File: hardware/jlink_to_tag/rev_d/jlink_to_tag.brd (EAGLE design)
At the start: 50.8 x 76.2 mm, 39 parts, among them J2 JLINK_6PIN_TAG-CON, J3 JLINK_6PIN_TAG-CON, J4 JLINK_6PIN_TAG-CON, J5 JLINK_6PIN_TAG-CON, J6 JLINK_6PIN_TAG-CON, J7 JLINK_6PIN_TAG-CON, J8 JLINK_6PIN_TAG-CON, J9 JLINK_6PIN_TAG-CON, U1 LT1763CS8-3.3

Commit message: getting more traces in
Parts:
- added D2, D3, D4, D5, D6, D7, D8, D9: BLUE, SparkFun-LED:LED-0603
- added R10, R11, R12, R13, R14, R15, R16, R9: 470, SparkFun-Passives:0603-RES
- added S10, S20, S4, S5, S6, S7, S8, S9: PTS645SM43SMTR92, switches:PTS645
- moved S1 62.0 mm to (78.7, 26.9)
- moved S2 62.0 mm to (73.2, 33.8)
- moved S3 62.0 mm to (83.8, 33.8)
- moved C1 21.5 mm to (-16.9, 49.3)
- moved C2 21.5 mm to (-12.2, 57.8)
- moved C3 21.5 mm to (-16.3, 57.8)
- moved D1 21.5 mm to (-13.8, 48.1)
- moved LOGO1 21.5 mm to (-15.4, 43.6)
- moved R1 21.5 mm to (-16.9, 47.2)
- moved U1 21.5 mm to (-15.1, 53.7)
- moved H2 20.2 mm to (60.2, 72.4)
- moved H4 20.2 mm to (60.2, 3.81)
- moved J6 20.2 mm to (60.2, 15.2)
- moved J7 20.2 mm to (60.2, 30.5)
- moved J9 20.2 mm to (60.2, 61.0)
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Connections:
- new net N$10: D8.C, R15.1
- new net N$11: D9.C, R16.1
- new net N$2: D2.C, R9.1
- new net N$5: D3.C, R10.1
- new net N$6: D4.C, R11.1
- new net N$7: D5.C, R12.1
- new net N$8: D6.C, R13.1
- new net N$9: D7.C, R14.1
- net !RST0: now also S4.3, S4.4
- net !RST1: now also S5.3, S5.4
- net !RST2: now also S6.3, S6.4
- net !RST3: now also S7.3, S7.4
- net !RST4: now also S8.3, S8.4
- net !RST5: now also S9.3, S9.4
- net !RST6: now also S10.3, S10.4
- net !RST7: now also S20.3, S20.4
- net EN0: now also D2.A
- net EN1: now also D3.A
- net EN2: now also D4.A
- net EN3: now also D5.A
- net EN4: now also D6.A
- net EN5: now also D7.A
- net EN6: now also D8.A
- net EN7: now also D9.A
- net GND: now also R10.2, R11.2, R12.2, R13.2, R14.2, R15.2, R16.2, R9.2, S10.1, S10.2, S20.1, S20.2, S4.1, S4.2, S5.1, S5.2, S6.1, S6.2, S7.1, S7.2, S8.1, S8.2, S9.1, S9.2
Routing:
- net GND: track 0.00 -> 71.5 mm, vias 0 -> 8
- net !RST3: track 0.00 -> 29.0 mm, vias 0 -> 1
- net SWO3: track 0.00 -> 20.5 mm, vias 0 -> 1
- net !RST0: track 15.2 -> 28.2 mm
- net SWDCLK3: track 0.00 -> 11.4 mm, vias 0 -> 1
- net SWDIO3: track 0.00 -> 10.9 mm, vias 0 -> 1
- net SWDIO0: track 0.00 -> 10.1 mm, vias 0 -> 1
- net SWO: track 81.8 -> 73.2 mm, vias 3 -> 4
- net !RST: track 89.6 -> 81.4 mm, vias 3 -> 4
- net !RST2: track 20.7 -> 28.6 mm
- net !RST7: track 0.00 -> 7.95 mm
- net !RST6: track 0.00 -> 7.95 mm
- net !RST5: track 0.00 -> 7.95 mm
- net !RST4: track 0.00 -> 7.95 mm
- net !RST1: track 20.7 -> 28.6 mm
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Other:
- board size 50.8 x 76.2 mm -> 64 x 76.2 mm
- board text added: "Reset Switches"

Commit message: board layout
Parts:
- removed C1, C2: 0.01uF, resistor:C0603
- removed C3: 10uF, SparkFun-Passives:EIA3216
- removed S1: EVQP2, switches:EVQP2
- removed S2, S3: TE_SSA12/SPDT, switches:TE_SSA12/SPDT
- added C4: 10nF, passives:0603_CAP
- added C5, C6: 4.7uF, passives:0603_CAP
- added J15: (no value), pinhead:2X03
- added S21, S22: STS121PC04, switches:STS121PC04
- added U2: MAX8887EZK33+T, chips:SOT-23-5
- U1: value LT1763CS8-3.3 -> 74HC4002PW; device linear-technology:SOIC8 -> chips:TSSOP-14/5MM
- moved R8 79.9 mm to (50.5, 67.3), turned to 90 degrees
- moved R7 67.5 mm to (50.0, 51.6), turned to 90 degrees
- moved R6 59.7 mm to (50.0, 36.3), turned to 90 degrees
- moved LOGO1 58.7 mm to (41.9, 55.9)
- moved R5 57.5 mm to (50.0, 21.1), turned to 90 degrees
- moved U1 54.4 mm to (37.1, 38.4), turned to 0 degrees
- moved R1 38.8 mm to (12.4, 72.6), turned to 270 degrees
- moved D1 34.3 mm to (10.2, 72.6)
- moved R2 27.3 mm to (14.0, 52.1), turned to 90 degrees
- moved R4 22.1 mm to (14.0, 21.6), turned to 90 degrees
- moved R3 22.1 mm to (14.0, 36.8), turned to 90 degrees
- turned D6 to 0 degrees
- turned D7 to 0 degrees
- turned D8 to 0 degrees
- turned D9 to 0 degrees
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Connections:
- removed net N$4: C2.2, U1.4
- new net N$1: C4.1, U2.4
- new net N$15: U1.1, U1.12
- net !RST: now also J15.3, S22.1; no longer S1.P$1, S1.P$3, S3.1
- net 3V3: now also C6.1, S21.1, U1.14, U2.5; no longer C2.1, C3.A, S2.1, U1.1, U1.2
- net 5V: now also C5.1, U2.1, U2.3; no longer C1.1, U1.5, U1.8
- net EN0: now also U1.13
- net EN1: now also U1.2
- net EN2: now also U1.3
- net EN3: now also U1.4
- net EN4: now also U1.5
- net EN5: now also U1.9
- net EN6: now also U1.10
- net EN7: now also U1.11
- net GND: now also C4.2, C5.2, C6.2, J15.5, U2.2; no longer C1.2, C3.C, S1.P$2, S1.P$4, U1.3, U1.6
- net SWDCLK: now also J15.4
- net SWDIO: now also J15.2, S22.2; no longer S3.IN
- net SWO: now also J15.6
- net VTREF: now also J15.1, S21.2; no longer S2.IN
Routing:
- net 3V3: track 0.00 -> 207.0 mm, vias 0 -> 1
- net VTREF: track 0.00 -> 202.2 mm, vias 0 -> 3
- net SWDIO: track 117.7 -> 241.4 mm, vias 4 -> 9
- net !RST: track 81.4 -> 201.7 mm, vias 4 -> 9
- net SWDCLK: track 93.9 -> 200.8 mm, vias 4 -> 9
- net SWO: track 73.2 -> 173.8 mm, vias 4 -> 9
- net EN3: track 3.39 -> 100.1 mm, vias 0 -> 4
- net !RST7: track 7.95 -> 85.1 mm, vias 0 -> 1
- net EN4: track 0.00 -> 76.4 mm, vias 0 -> 5
- net EN2: track 3.39 -> 78.9 mm, vias 0 -> 3
- net EN1: track 3.97 -> 78.6 mm, vias 0 -> 5
- net EN7: track 0.00 -> 69.7 mm, vias 0 -> 6
- net !RST6: track 7.95 -> 67.5 mm, vias 0 -> 2
- net EN6: track 0.00 -> 58.0 mm, vias 0 -> 6
- net !RST0: track 28.2 -> 83.9 mm
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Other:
- board text added: "2016/11/01"
- board text added: "Brad Campbell"
- board text added: "CLK"
- board text added: "Channel Select"
- board text added: "D"
- board text added: "GND"
- board text added: "IO"
- board text added: "OCTOTAG"
- board text added: "POWER"
- board text added: "SWO"
- board text added: "VCC"
- board text removed: "2015/10/26"
- board text removed: "C"
- board text removed: "JTAG-TC"
- board text removed: "NK,BC"
- board text removed: "PWR"
- board text removed: "RESET"

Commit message: started renumber rev d
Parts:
- R10, R11, R12, R13, R14, R15, R16: value 470 -> 1k
- R2, R3, R4, R5, R6, R7, R8: value 1k -> 470
- moved R9 46.7 mm to (55.4, 64.5)
- moved R5 41.5 mm to (8.64, 18.8)
- moved R8 18.7 mm to (55.4, 49.3), turned to 270 degrees
- moved R6 18.3 mm to (55.4, 18.8), turned to 270 degrees
- moved R7 18.3 mm to (55.4, 34.0), turned to 270 degrees
- moved R2 13.5 mm to (8.64, 64.5), turned to 270 degrees
- moved R3 13.5 mm to (8.64, 49.3)
- moved R4 13.5 mm to (8.64, 34.0)
- moved R12 6.02 mm to (14.0, 21.6)
- moved R10 6.02 mm to (14.0, 52.1)
- moved R11 6.02 mm to (14.0, 36.8)
- moved R13 5.80 mm to (50.0, 21.1), turned to 90 degrees
- moved R14 5.80 mm to (50.0, 36.3), turned to 90 degrees
- moved R15 5.80 mm to (50.0, 51.6), turned to 90 degrees
- moved R16 5.58 mm to (50.5, 67.3), turned to 90 degrees
- renumbered C4 to C1, C5 to C2, C6 to C3
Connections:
- net EN1: now also R10.1; no longer R2.1
- net EN2: now also R11.1; no longer R3.1
- net EN3: now also R12.1; no longer R4.1
- net EN4: now also R13.1; no longer R5.1
- net EN5: now also R14.1; no longer R6.1
- net EN6: now also R15.1; no longer R7.1
- net EN7: now also R16.1; no longer R8.1
- net N$10: now also R8.1; no longer R15.1
- net N$11: now also R9.1; no longer R16.1
- net N$2: now also R2.1; no longer R9.1
- net N$5: now also R3.1; no longer R10.1
- net N$6: now also R4.1; no longer R11.1
- net N$7: now also R5.1; no longer R12.1
- net N$8: now also R6.1; no longer R13.1
- net N$9: now also R7.1; no longer R14.1

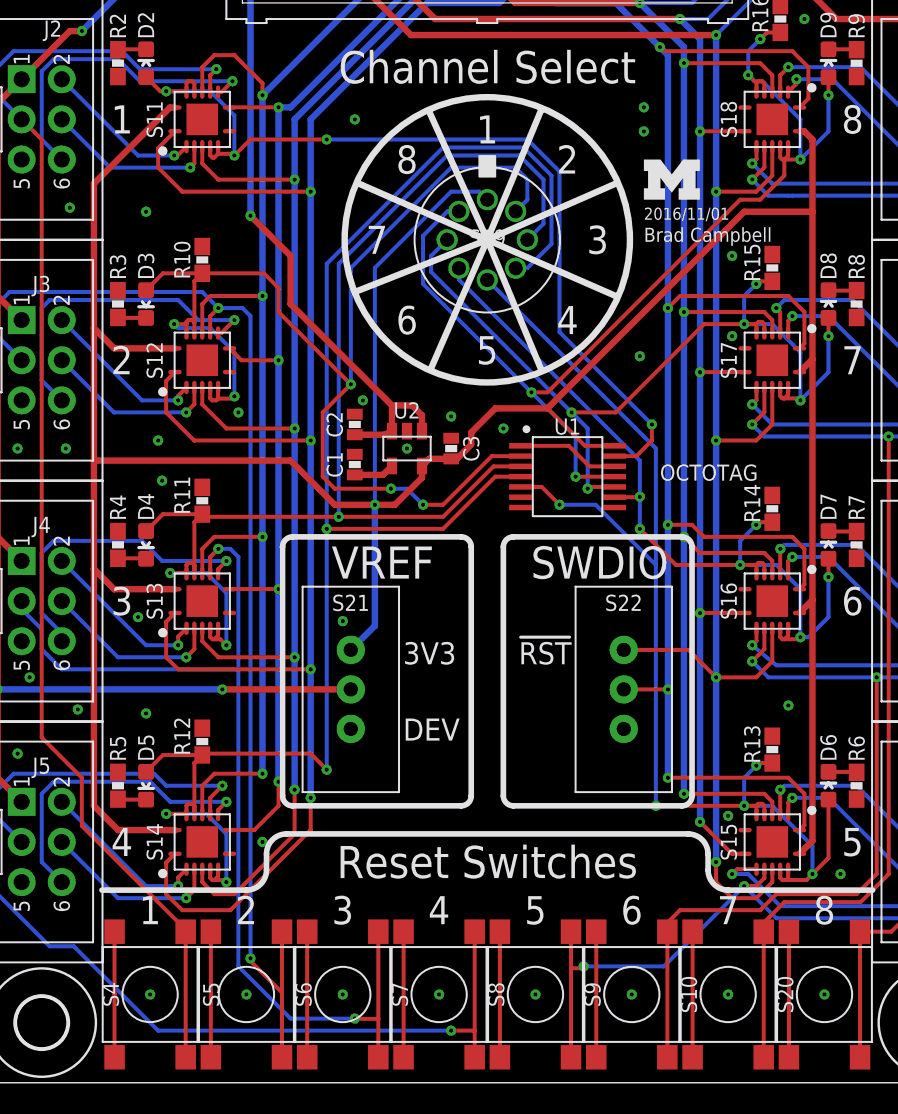
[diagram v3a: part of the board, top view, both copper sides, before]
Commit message: Order switches
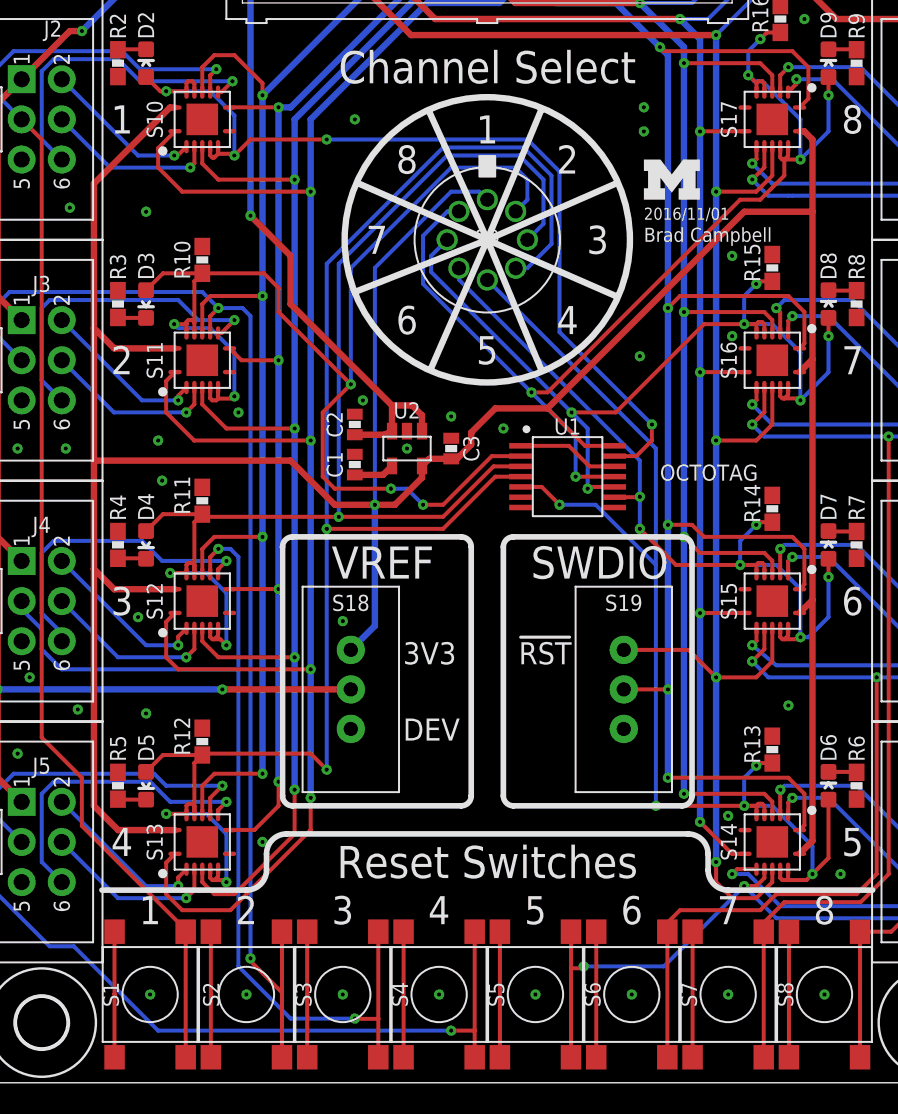
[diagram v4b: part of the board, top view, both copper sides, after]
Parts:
- removed S20: PTS645SM43SMTR92, switches:PTS645
- removed S21, S22: STS121PC04, switches:STS121PC04
- added S1, S2, S3: PTS645SM43SMTR92, switches:PTS645
- S10: value PTS645SM43SMTR92 -> SN74AHC4066-RGY; device switches:PTS645 -> switches:S-PVQFN-N14-3.5MM
- S18: value SN74AHC4066-RGY -> STS121PC04; device switches:S-PVQFN-N14-3.5MM -> switches:STS121PC04
- S19: value RM100772BCB -> STS121PC04; device switches:RM-SWITCH -> switches:STS121PC04
- S9: value PTS645SM43SMTR92 -> RM100772BCB; device switches:PTS645 -> switches:RM-SWITCH
- moved S10 64.6 mm to (14.0, 61.0), turned to 0 degrees
- moved S9 48.6 mm to (32.0, 53.3), turned to 0 degrees
- moved S18 44.9 mm to (23.4, 24.9), turned to 270 degrees
- moved S14 36.1 mm to (50.0, 15.2), turned to 180 degrees
- moved S19 29.7 mm to (40.6, 24.9), turned to 270 degrees
- moved S6 18.3 mm to (41.1, 5.59)
- moved S8 18.3 mm to (53.3, 5.59)
- moved S4 18.3 mm to (29.0, 5.59)
- moved S5 18.3 mm to (35.1, 5.59)
- moved S7 18.3 mm to (47.2, 5.59)
- moved S11 15.2 mm to (14.0, 45.7)
- moved S17 15.2 mm to (50.0, 61.0)
- moved S13 15.2 mm to (14.0, 15.2)
- moved S15 15.2 mm to (50.0, 30.5)
- moved S12 15.2 mm to (14.0, 30.5)
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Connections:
- net !RST: now also S10.11, S19.1; no longer S18.11, S22.1
- net !RST0: now also S1.3, S1.4, S10.10; no longer S11.10, S4.3, S4.4
- net !RST1: now also S11.10, S2.3, S2.4; no longer S12.10, S5.3, S5.4
- net !RST2: now also S12.10, S3.3, S3.4; no longer S13.10, S6.3, S6.4
- net !RST3: now also S13.10, S4.3, S4.4; no longer S14.10, S7.3, S7.4
- net !RST4: now also S14.10, S5.3, S5.4; no longer S15.10, S8.3, S8.4
- net !RST5: now also S15.10, S6.3, S6.4; no longer S16.10, S9.3, S9.4
- net !RST6: now also S16.10, S7.3, S7.4; no longer S10.3, S10.4, S17.10
- net !RST7: now also S17.10, S8.3, S8.4; no longer S18.10, S20.3, S20.4
- net 3V3: now also S10.14, S18.1, S9.C; no longer S18.14, S19.C, S21.1
- net EN0: now also S10.12, S10.13, S10.5, S10.6; no longer S11.12, S11.13, S11.5, S11.6
- net EN1: now also S11.12, S11.13, S11.5, S11.6, S9.1; no longer S12.12, S12.13, S12.5, S12.6, S19.1
- net EN2: now also S12.12, S12.13, S12.5, S12.6, S9.2; no longer S13.12, S13.13, S13.5, S13.6, S19.2
- net EN3: now also S13.12, S13.13, S13.5, S13.6, S9.3; no longer S14.12, S14.13, S14.5, S14.6, S19.3
- net EN4: now also S14.12, S14.13, S14.5, S14.6, S9.4; no longer S15.12, S15.13, S15.5, S15.6, S19.4
- net EN5: now also S15.12, S15.13, S15.5, S15.6, S9.5; no longer S16.12, S16.13, S16.5, S16.6, S19.5
- net EN6: now also S16.12, S16.13, S16.5, S16.6, S9.6; no longer S17.12, S17.13, S17.5, S17.6, S19.6
- net EN7: now also S17.12, S17.13, S17.5, S17.6, S9.7; no longer S18.12, S18.13, S18.5, S18.6, S19.7
- net GND: now also S1.1, S1.2, S10.7, S2.1, S2.2, S3.1, S3.2; no longer S10.1, S10.2, S18.7, S20.1, S20.2, S9.1, S9.2
- net SWDCLK: now also S10.4; no longer S18.4
- net SWDCLK0: now also S10.3; no longer S11.3
- net SWDCLK1: now also S11.3; no longer S12.3
- net SWDCLK2: now also S12.3; no longer S13.3
- net SWDCLK3: now also S13.3; no longer S14.3
- net SWDCLK4: now also S14.3; no longer S15.3
- net SWDCLK5: now also S15.3; no longer S16.3
- net SWDCLK6: now also S16.3; no longer S17.3
- net SWDCLK7: now also S17.3; no longer S18.3
- net SWDIO: now also S10.1, S19.2; no longer S18.1, S22.2
- net SWDIO0: now also S10.2; no longer S11.2
- net SWDIO1: now also S11.2; no longer S12.2
- net SWDIO2: now also S12.2; no longer S13.2
- net SWDIO3: now also S13.2; no longer S14.2
- net SWDIO4: now also S14.2; no longer S15.2
- net SWDIO5: now also S15.2; no longer S16.2
- net SWDIO6: now also S16.2; no longer S17.2
- net SWDIO7: now also S17.2; no longer S18.2
- net SWO: now also S10.8; no longer S18.8
- net SWO0: now also S10.9; no longer S11.9
- net SWO1: now also S11.9; no longer S12.9
- net SWO2: now also S12.9; no longer S13.9
- net SWO3: now also S13.9; no longer S14.9
- net SWO4: now also S14.9; no longer S15.9
- net SWO5: now also S15.9; no longer S16.9
- net SWO6: now also S16.9; no longer S17.9
- net SWO7: now also S17.9; no longer S18.9
- net VTREF: now also S18.2; no longer S21.2
